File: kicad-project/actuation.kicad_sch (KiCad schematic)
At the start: 44 parts

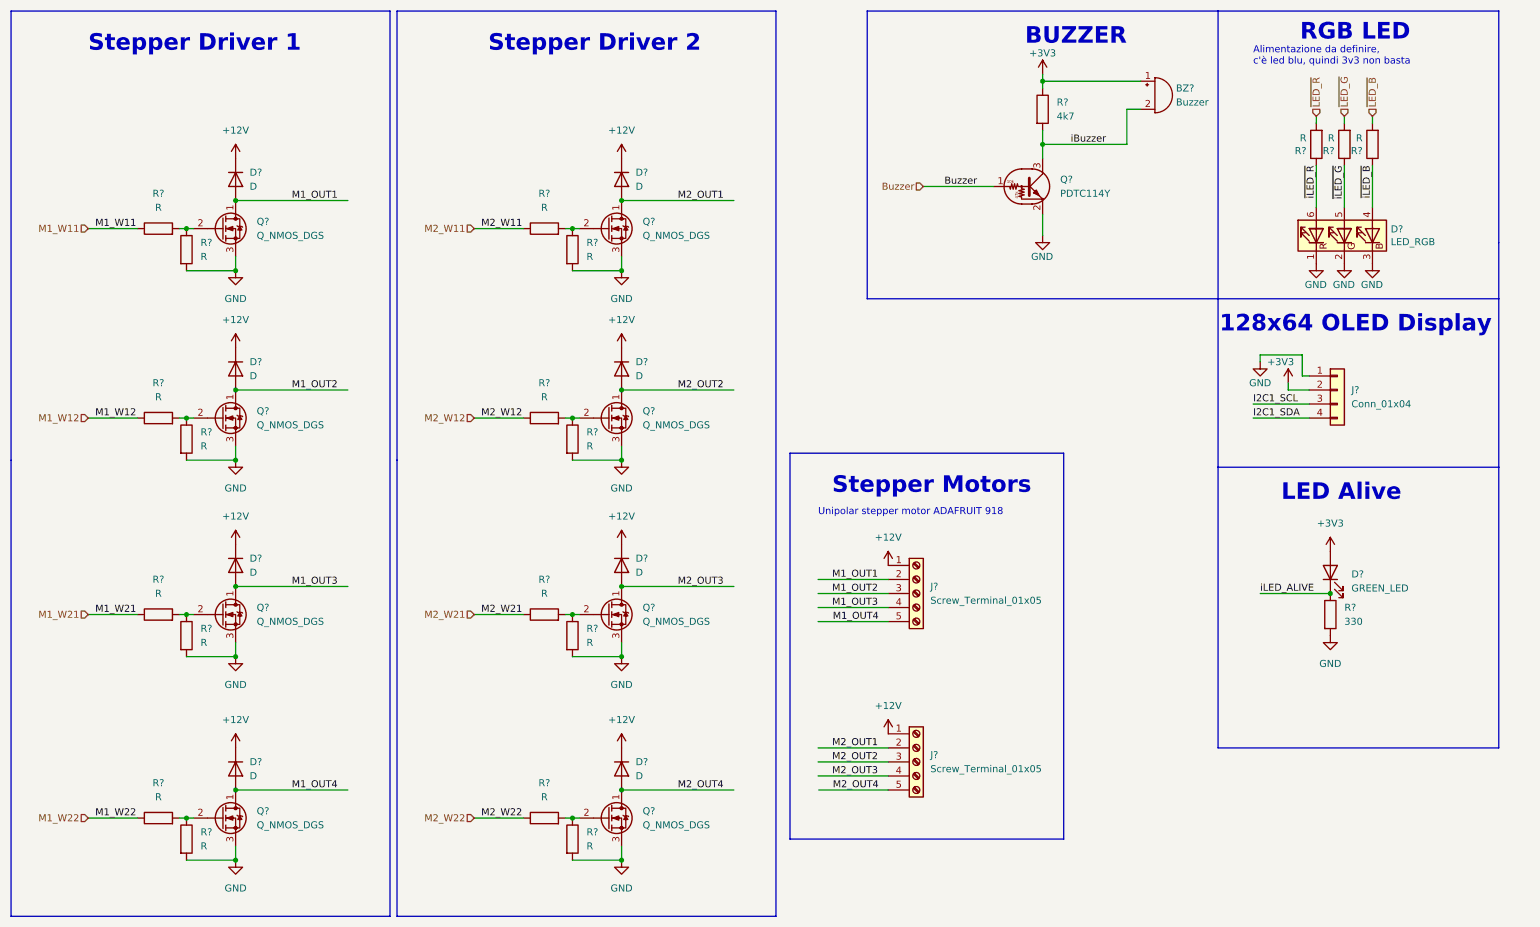
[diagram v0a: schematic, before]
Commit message: hw: add footprints for resistors and capacitors and re-add specs documant that was deleted
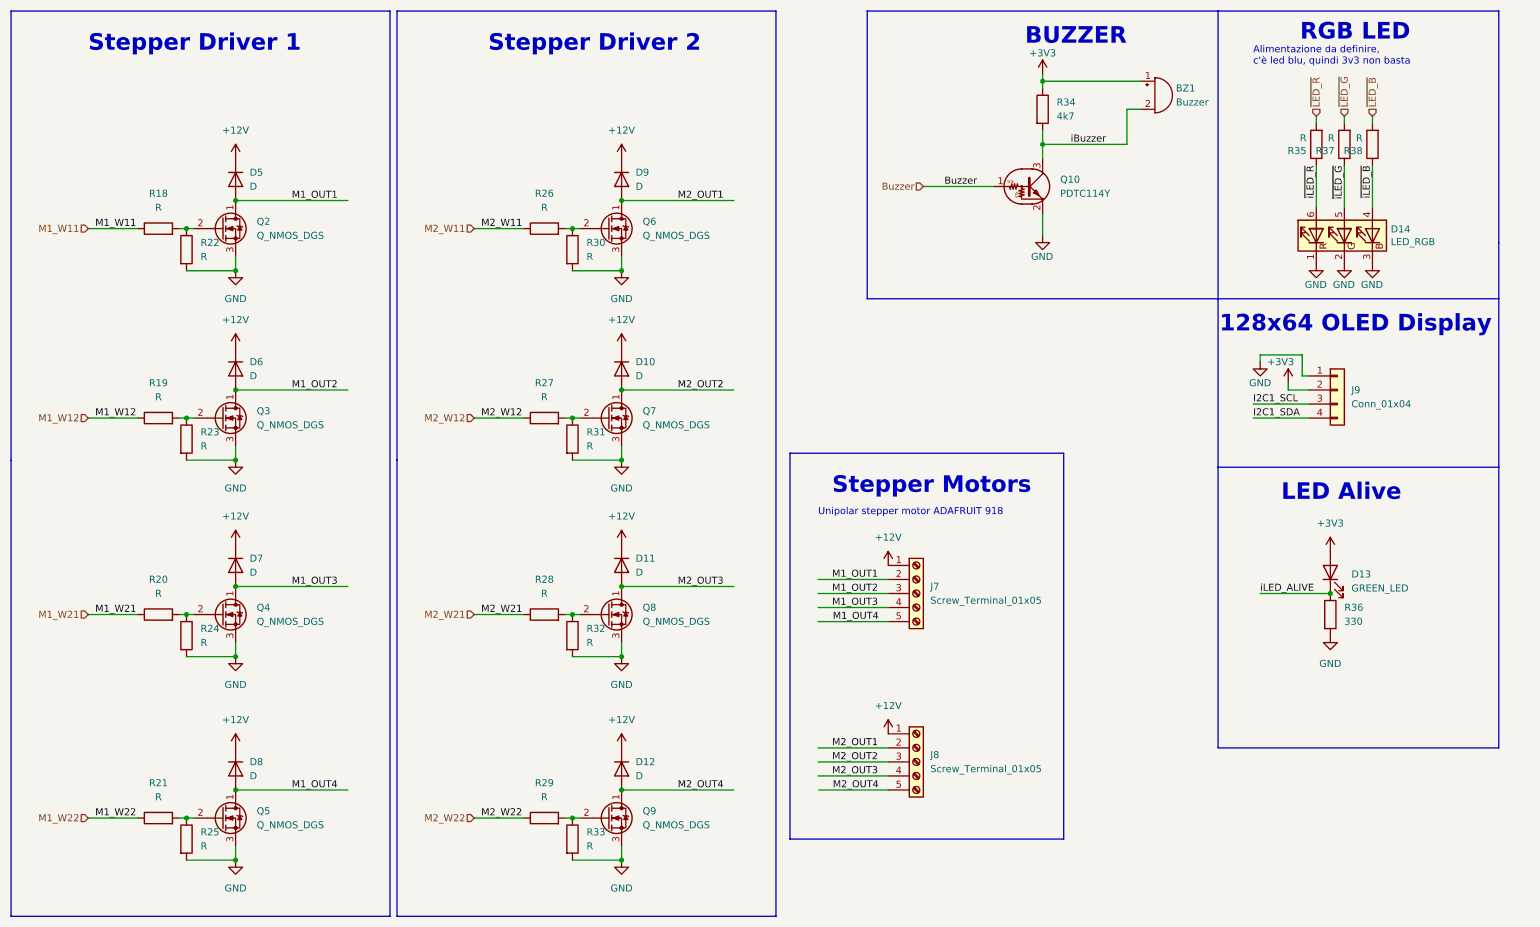
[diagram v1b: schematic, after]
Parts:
- BZ1: renamed from BZ?; footprint (none) -> Buzzer_Beeper:Buzzer_12x9.5RM7.6
- D13: renamed from D?; footprint (none) -> LED_SMD:LED_0603_1608Metric
- D14: renamed from D?; footprint (none) -> LED_SMD:LED_RGB_1210
- J7, J8: renamed from J?; footprint (none) -> TerminalBlock_TE-Connectivity:TerminalBlock_TE_282834-5_1x05_P2.54mm_Horizontal
- J9: renamed from J?; footprint (none) -> Connector_PinHeader_2.54mm:PinHeader_1x04_P2.54mm_Vertical_SMD_Pin1Left
- R18, R19, R20, R21, R22, R23, R24, R25, R26, R27, R28, R29, R30, R31, R32, R33, R34, R35, R36, R37, R38: renamed from R?; footprint (none) -> Resistor_SMD:R_0603_1608Metric
- gave numbers to parts that had none: 17

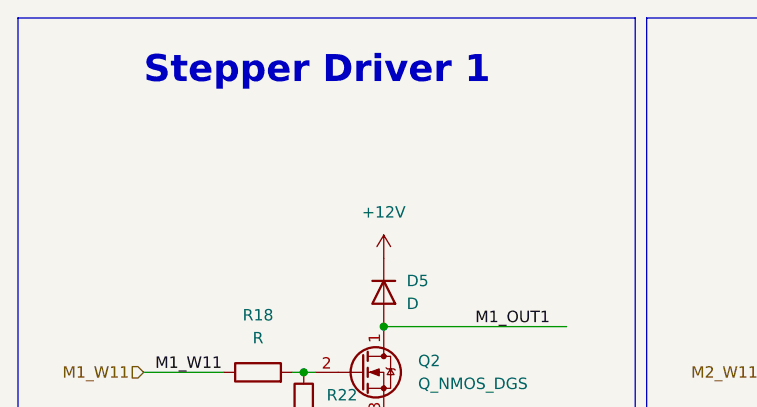
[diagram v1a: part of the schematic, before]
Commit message: hw: update root pin and usb connector
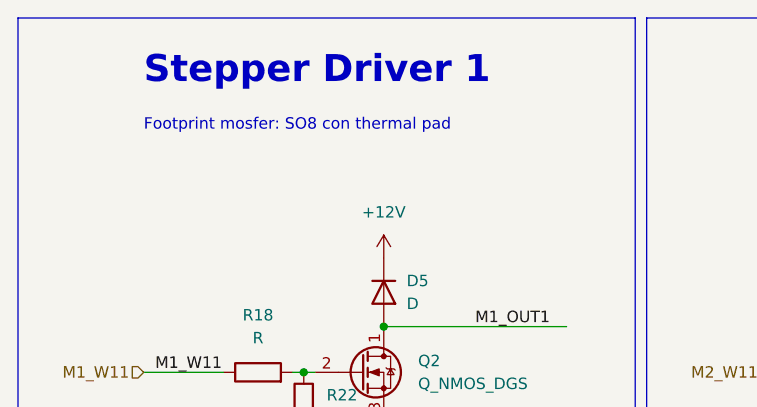
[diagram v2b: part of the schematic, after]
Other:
- note added: "Footprint mosfer: SO8 con thermal pad"
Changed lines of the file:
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@@
     (stroke (width 0) (type default) (color 0 0 0 0))
+  )
+  (text "Footprint mosfer: SO8 con thermal pad" (at 27.94 26.67 0)
+    (effects (font (size 1.27 1.27)) (justify left bottom))
   )
   (text "LED Alive\n" (at 243.84 102.87 0)

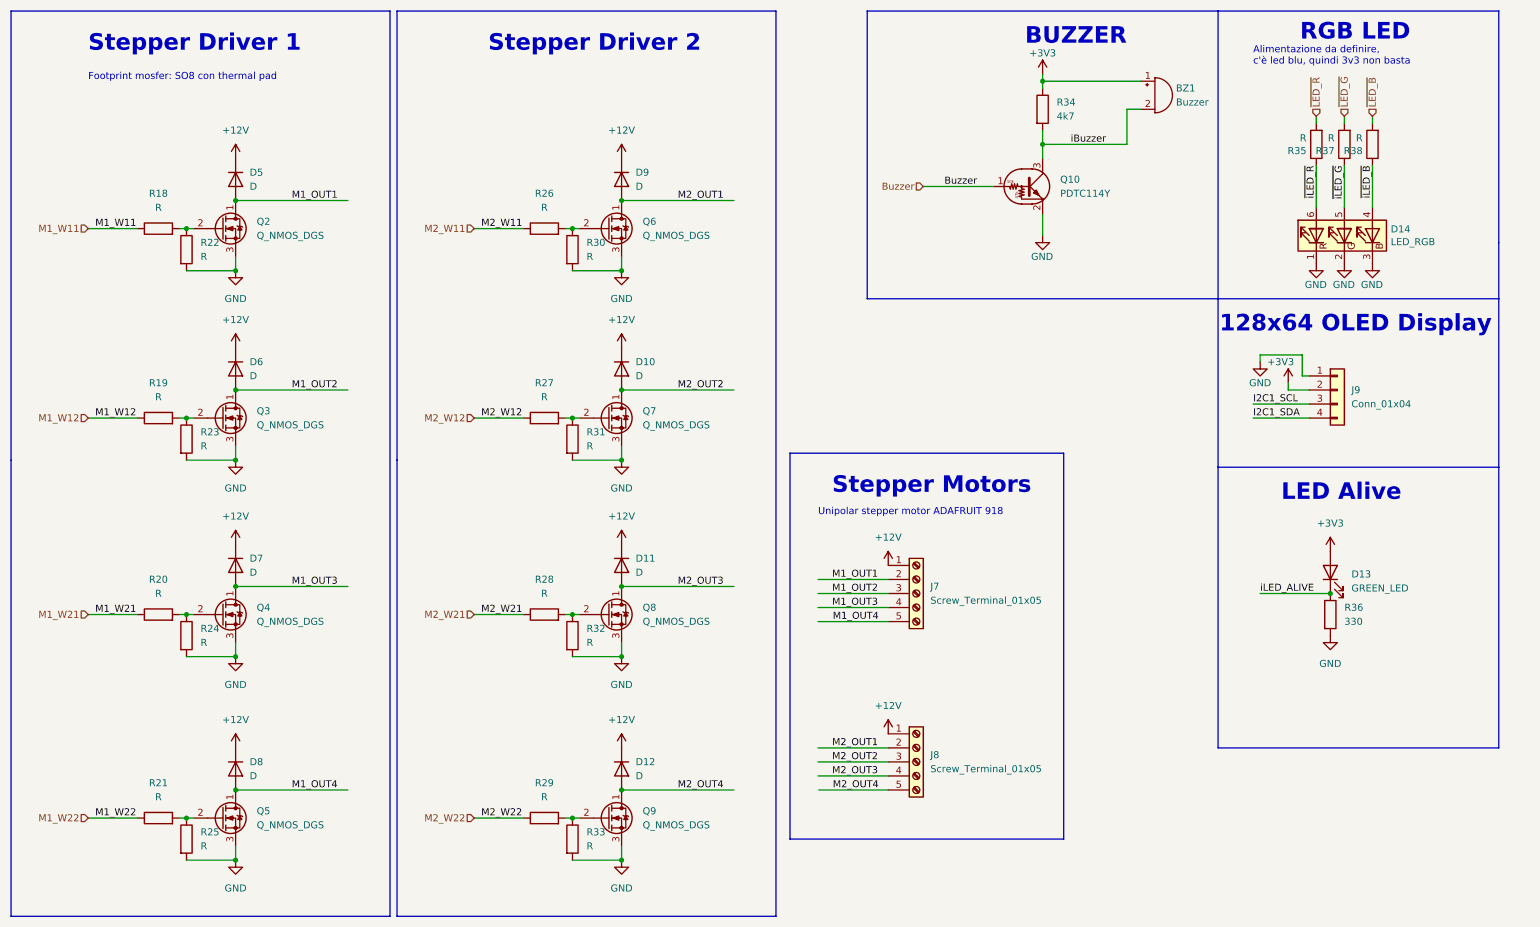
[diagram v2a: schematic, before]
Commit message: hw: rgb led with NPN
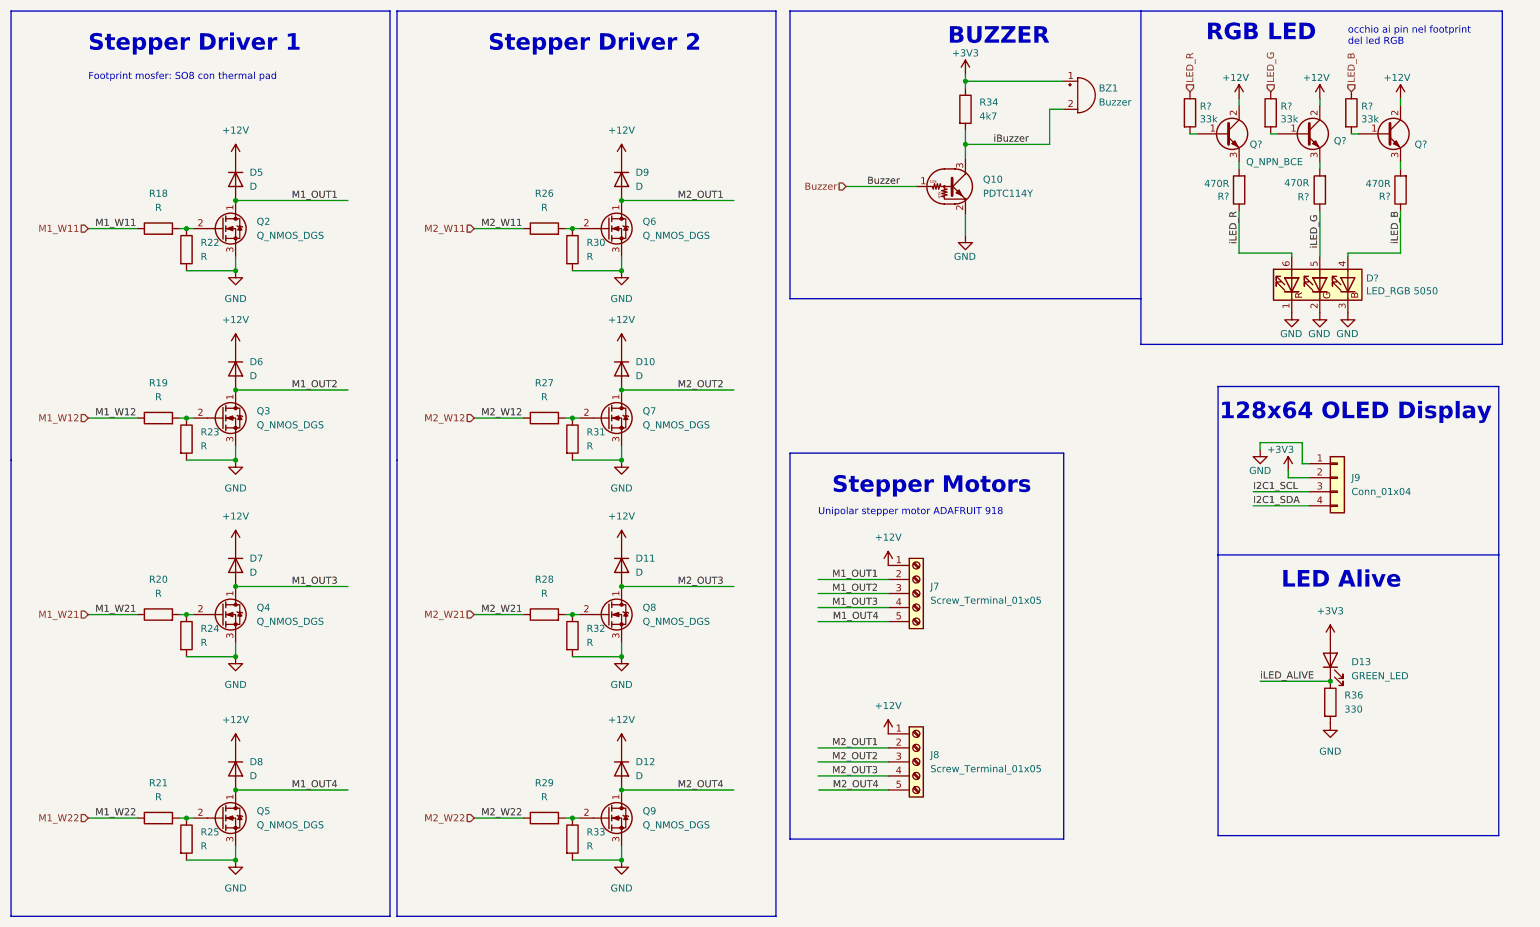
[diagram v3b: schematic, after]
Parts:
- removed D14: LED_RGB, LED_SMD:LED_RGB_1210, symbol Device:LED_RGB
- removed R35, R37, R38: R, Resistor_SMD:R_0603_1608Metric, symbol Device:R
- added D?: LED_RGB 5050, LED_SMD:LED_RGB_1210, symbol Device:LED_RGB
- added Q? (x2): ~, symbol Device:Q_NPN_BCE
- added Q?: Q_NPN_BCE, symbol Device:Q_NPN_BCE
- added R? (x3): 33k, Resistor_SMD:R_0603_1608Metric, symbol Device:R
- added R? (x3): 470R, Resistor_SMD:R_0603_1608Metric, symbol Device:R
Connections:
- net +12V: now also Q?.2 (C), Q?.2 (C), Q?.2 (C)
- net GND: now also D?.1 (RK), D?.2 (GK), D?.3 (BK)
- new net: Q?.1 (B), R?.2 (x3)
- new net: Q?.3 (E), R?.2 (x3)
- new net LED_B: R?.1
- new net LED_G: R?.1
- new net LED_R: R?.1
- new net iLED_B: D?.4 (BA), R?.1
- new net iLED_G: D?.5 (GA), R?.1
- new net iLED_R: D?.6 (RA), R?.1
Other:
- note added: "occhio ai pin nel footprint del led RGB"
- note removed: "Alimentazione da definire, c'è led blu, quindi 3v3 non basta"
- moved on the sheet: BZ1, D13, J9, Q10, R34, R36

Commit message: hw: part of last checks and footprint assignments
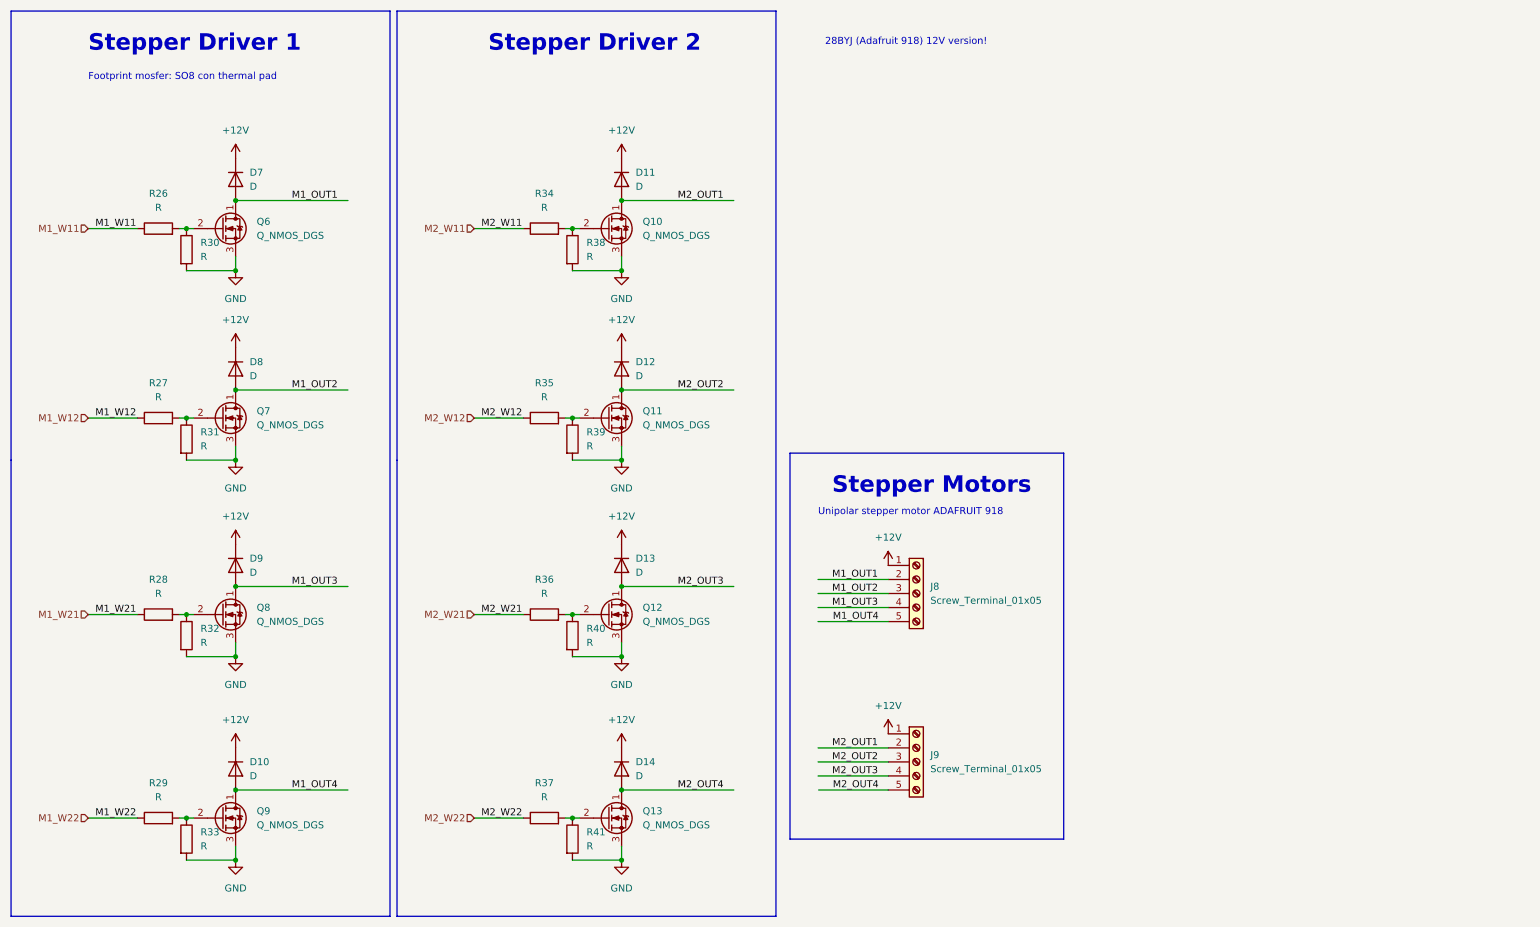
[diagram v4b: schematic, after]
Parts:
- removed BZ1: Buzzer, Buzzer_Beeper:Buzzer_12x9.5RM7.6, symbol Device:Buzzer
- removed D13: GREEN_LED, LED_SMD:LED_0603_1608Metric, symbol Device:LED
- removed D?: LED_RGB 5050, LED_SMD:LED_RGB_1210, symbol Device:LED_RGB
- removed J9: Conn_01x04, Connector_PinHeader_2.54mm:PinHeader_1x04_P2.54mm_Vertical_SMD_Pin1Left, symbol Connector_Generic:Conn_01x04
- removed Q10: PDTC114Y, symbol Transistor_BJT:DTC114Y
- removed Q? (x2): ~, symbol Device:Q_NPN_BCE
- removed Q?: Q_NPN_BCE, symbol Device:Q_NPN_BCE
- removed R34: 4k7, Resistor_SMD:R_0603_1608Metric, symbol Device:R
- removed R36: 330, Resistor_SMD:R_0603_1608Metric, symbol Device:R
- removed R? (x3): 33k, Resistor_SMD:R_0603_1608Metric, symbol Device:R
- removed R? (x3): 470R, Resistor_SMD:R_0603_1608Metric, symbol Device:R
- renumbered D8 to D10, D9 to D11, D10 to D12, D11 to D13, D12 to D14, D5 to D7, D6 to D8, D7 to D9, J7 to J8, J8 to J9, Q6 to Q10, Q7 to Q11, Q8 to Q12, Q9 to Q13, Q2 to Q6, Q3 to Q7, Q4 to Q8, Q5 to Q9, R18 to R26, R19 to R27, R20 to R28, R21 to R29, R22 to R30, R23 to R31, R24 to R32, R25 to R33, R26 to R34, R27 to R35, R28 to R36, R29 to R37, R30 to R38, R31 to R39, R32 to R40, R33 to R41
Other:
- note added: "28BYJ (Adafruit 918) 12V version!"
- note removed: "128x64 OLED Display"
- note removed: "BUZZER"
- note removed: "LED Alive"
- note removed: "RGB LED"
- note removed: "occhio ai pin nel footprint del led RGB"

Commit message: hw: schematic updates
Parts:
- removed J8, J9: Screw_Terminal_01x05, TerminalBlock_TE-Connectivity:TerminalBlock_TE_282834-5_1x05_P2.54mm_Horizontal, symbol Connector:Screw_Terminal_01x05
- removed R27, R28, R29, R31, R32, R33, R34, R35, R36, R37, R38, R39, R40, R41: R, Resistor_SMD:R_0603_1608Metric, symbol Device:R
- added J?: Motor 2, Connector_JST:JST_XH_S5B-XH-A_1x05_P2.50mm_Horizontal, symbol Connector_Generic:Conn_01x05
- added J?: Motor 1, Connector_JST:JST_XH_S5B-XH-A_1x05_P2.50mm_Horizontal, symbol Connector_Generic:Conn_01x05
- added R? (x7): 10k, Resistor_SMD:R_0603_1608Metric, symbol Device:R
- added R? (x7): 22, Resistor_SMD:R_0603_1608Metric, symbol Device:R
- D10, D11, D12, D13, D14, D7, D8, D9: value D -> CGRA4007; footprint (none) -> Diode_SMD:D_SMA
- Q10, Q11, Q12, Q13, Q6, Q7, Q8, Q9: value Q_NMOS_DGS -> SI2300DS; footprint (none) -> Package_TO_SOT_SMD:SOT-23
- R26: value R -> 22
- R30: value R -> 10k
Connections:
- net +12V: now also J?.1 (Pin_1), J?.1 (Pin_1)
- net GND: now also R?.2, R?.2, R?.2, R?.2, R?.2, R?.2, R?.2
- net M1_OUT1: now also J?.2 (Pin_2)
- net M1_OUT2: now also J?.3 (Pin_3)
- net M1_OUT3: now also J?.4 (Pin_4)
- net M1_OUT4: now also J?.5 (Pin_5)
- net M1_W12: now also R?.1
- net M1_W21: now also R?.1
- net M1_W22: now also R?.1
- net M2_OUT1: now also J?.2 (Pin_2)
- net M2_OUT2: now also J?.3 (Pin_3)
- net M2_OUT3: now also J?.4 (Pin_4)
- net M2_OUT4: now also J?.5 (Pin_5)
- net M2_W11: now also R?.1
- net M2_W12: now also R?.1
- net M2_W21: now also R?.1
- net M2_W22: now also R?.1
- net at Q12.2 (G): now also R?.1, R?.2
- net at Q11.2 (G): now also R?.1, R?.2
- net at Q9.2 (G): now also R?.1, R?.2
- net at Q10.2 (G): now also R?.1, R?.2
- net at Q7.2 (G): now also R?.1, R?.2
- net at Q8.2 (G): now also R?.1, R?.2
- net at Q13.2 (G): now also R?.1, R?.2
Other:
- note added: "Unipolar stepper motor 28BYJ (ADAFRUIT 918) 12V version"
- note removed: "28BYJ (Adafruit 918) 12V version!"
- note removed: "Footprint mosfer: SO8 con thermal pad"
- note removed: "Unipolar stepper motor ADAFRUIT 918"

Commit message: commit anonimo di thimas
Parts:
- gave numbers to parts that had none: 16
- renumbered D8 to D10, D9 to D11, D10 to D12, D11 to D13, D12 to D14, D13 to D15, D14 to D16, D7 to D9, R26 to R24, R30 to R28
